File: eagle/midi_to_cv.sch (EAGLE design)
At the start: 57 parts, among them IC1 TL084P, IC2 TL084P, U1 ATMEGA328P_PDIP

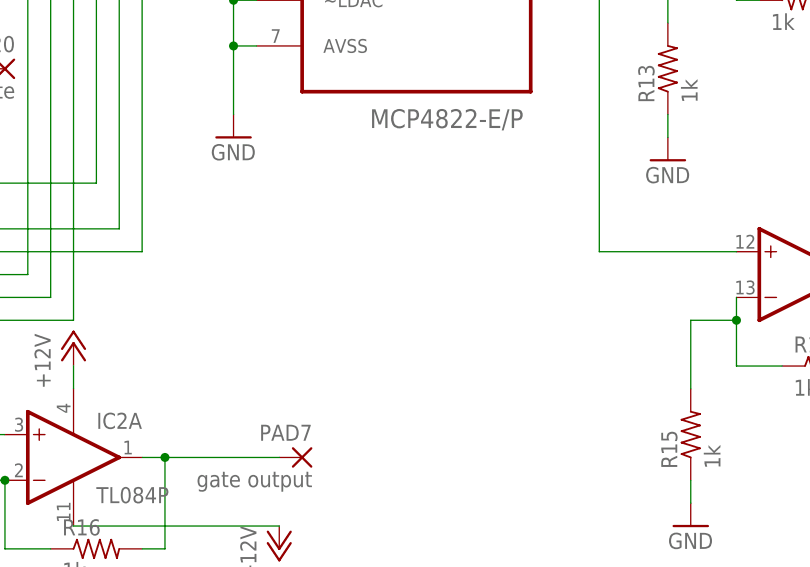
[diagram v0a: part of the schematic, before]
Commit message: will add iscp header
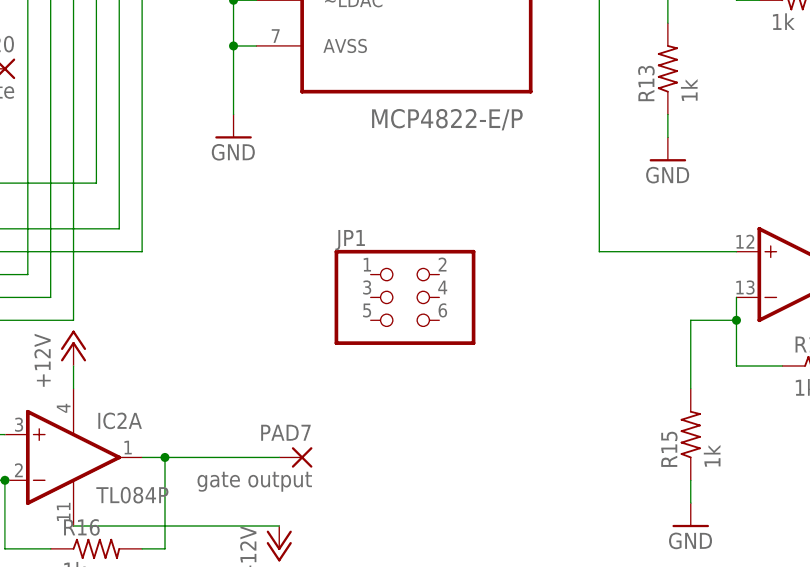
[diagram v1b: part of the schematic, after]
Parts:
- added JP1: (no value), pinhead:PINHD-2X3
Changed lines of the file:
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@@
 <part name="PAD21" library="wirepad" deviceset="2,54/0,9" device="" value="gate"/>
 <part name="PAD22" library="wirepad" deviceset="2,54/0,9" device="" value="gate"/>
+<part name="JP1" library="pinhead" deviceset="PINHD-2X3" device=""/>
 </parts>
 <sheets>
@@
 <instance part="PAD21" gate="1" x="58.42" y="40.64" rot="MR0"/>
 <instance part="PAD22" gate="1" x="50.8" y="38.1" rot="MR0"/>
+<instance part="JP1" gate="A" x="104.14" y="20.32"/>
 </instances>
 <busses>
